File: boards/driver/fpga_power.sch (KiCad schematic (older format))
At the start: 6 parts

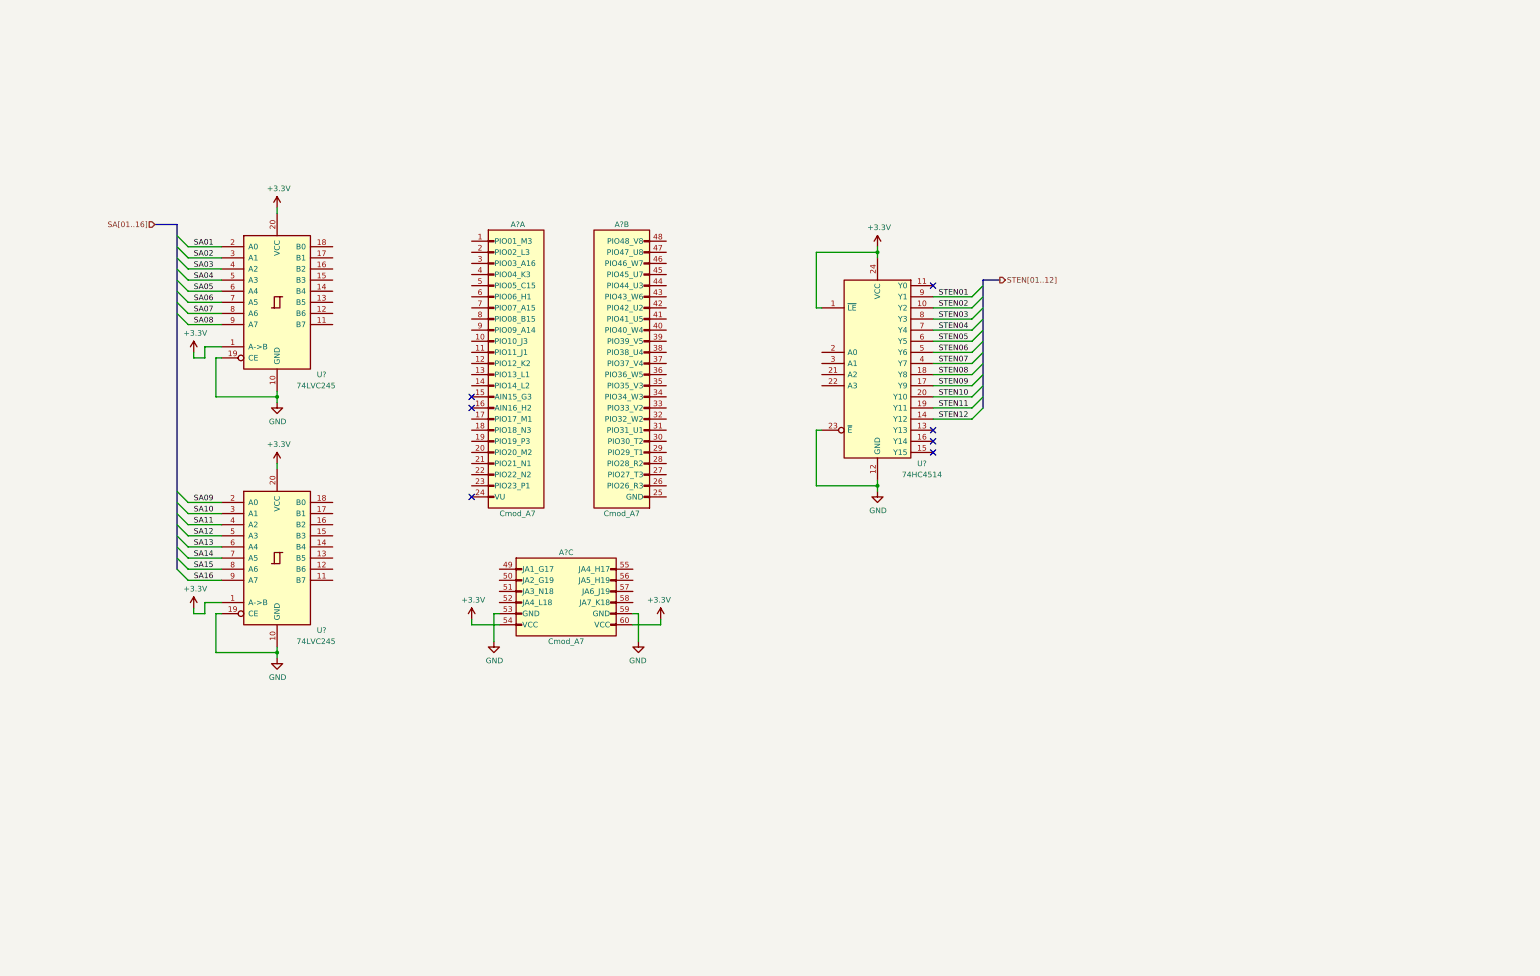
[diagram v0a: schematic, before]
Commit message: Driver boards: filled out all of the FPGA connections. Power circuits to still be defined.
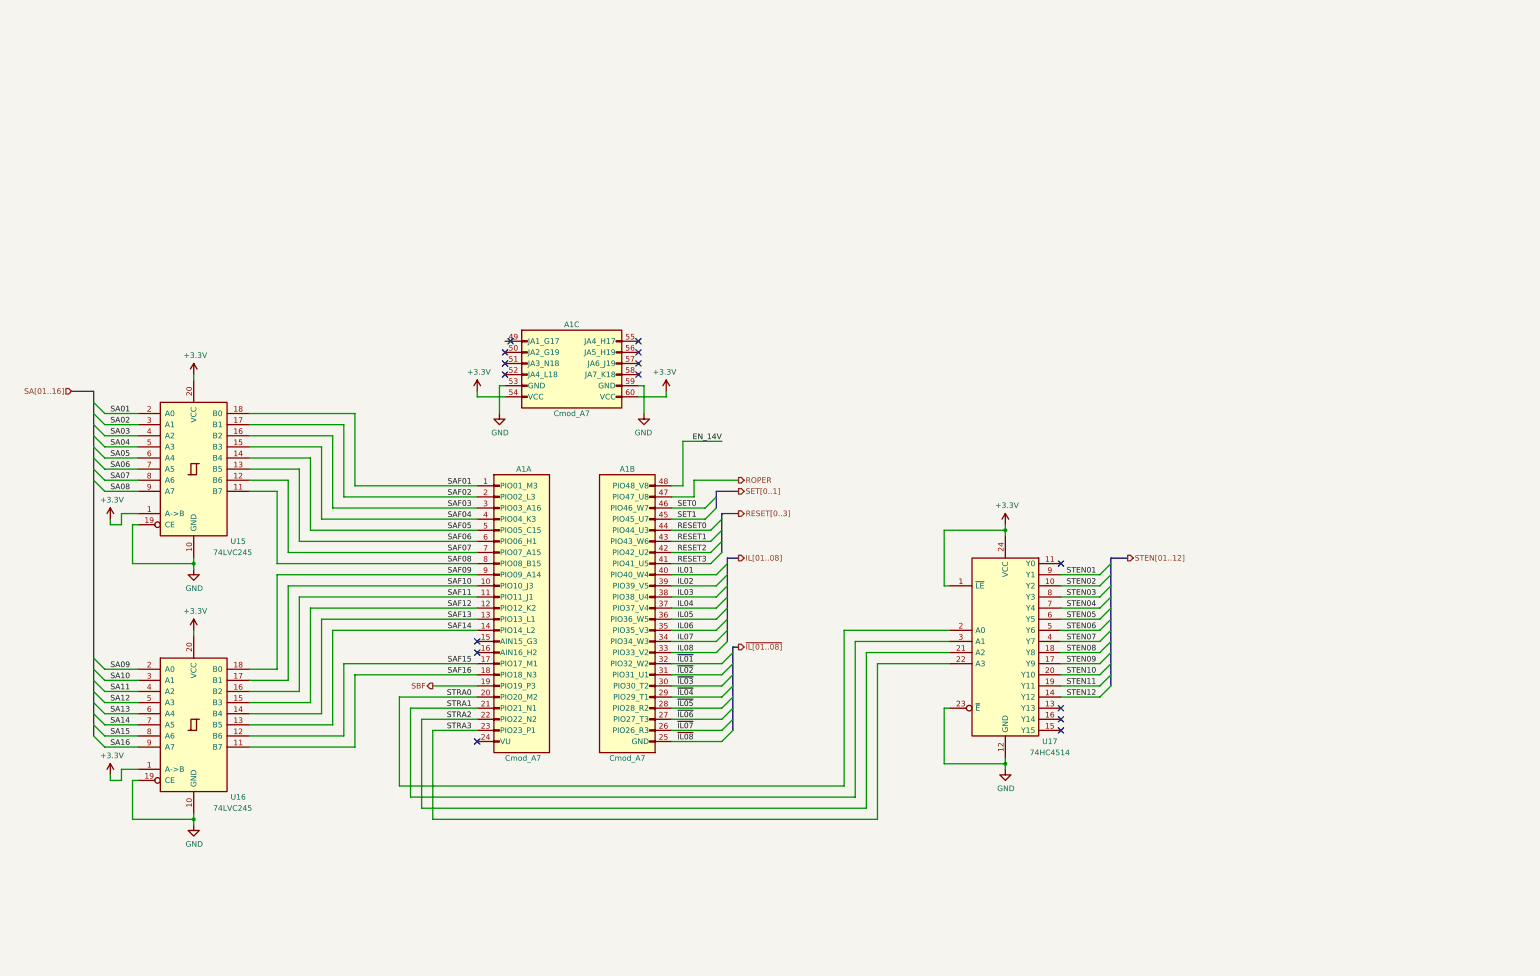
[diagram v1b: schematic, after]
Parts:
- gave numbers to parts that had none: 4
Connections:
- net SAF01: now reaches A1.1 (PIO01_M3)
- net SAF01: now also U15.18 (B0)
- net SAF10: now reaches A1.10 (PIO10_J3)
- net SAF10: now also U16.17 (B1)
- net SAF11: now reaches A1.11 (PIO11_J1)
- net SAF11: now also U16.16 (B2)
- net SAF12: now reaches A1.12 (PIO12_K2)
- net SAF12: now also U16.15 (B3)
- net SAF13: now reaches A1.13 (PIO13_L1)
- net SAF13: now also U16.14 (B4)
- net SAF14: now reaches A1.14 (PIO14_L2)
- net SAF14: now also U16.13 (B5)
- net SAF15: now reaches A1.17 (PIO17_M1)
- net SAF15: now also U16.12 (B6)
- net SAF16: now reaches A1.18 (PIO18_N3)
- net SAF16: now also U16.11 (B7)
- net SBF: now reaches A1.19 (PIO19_P3)
- net SAF02: now reaches A1.2 (PIO02_L3)
- net SAF02: now also U15.17 (B1)
- net STRA0: now reaches A1.20 (PIO20_M2)
- net STRA0: now also U17.2 (A0)
- net STRA1: now reaches A1.21 (PIO21_N1)
- net STRA1: now also U17.3 (A1)
- net STRA2: now reaches A1.22 (PIO22_N2)
- net STRA2: now also U17.21 (A2)
- net STRA3: now reaches A1.23 (PIO23_P1)
- net STRA3: now also U17.22 (A3)
- net SAF03: now reaches A1.3 (PIO03_A16)
- net SAF03: now also U15.16 (B2)
- net SAF04: now reaches A1.4 (PIO04_K3)
- net SAF04: now also U15.15 (B3)
- net SAF05: now reaches A1.5 (PIO05_C15)
- net SAF05: now also U15.14 (B4)
- net SAF06: now reaches A1.6 (PIO06_H1)
- net SAF06: now also U15.13 (B5)
- net SAF07: now reaches A1.7 (PIO07_A15)
- net SAF07: now also U15.12 (B6)
- net SAF08: now reaches A1.8 (PIO08_B15)
- net SAF08: now also U15.11 (B7)
- net SAF09: now reaches A1.9 (PIO09_A14)
- net SAF09: now also U16.18 (B0)
- net ~IL08: now reaches A1.25 (GND)
- net ~IL07: now reaches A1.26 (PIO26_R3)
- net ~IL06: now reaches A1.27 (PIO27_T3)
- net ~IL05: now reaches A1.28 (PIO28_R2)
- net ~IL04: now reaches A1.29 (PIO29_T1)
- net ~IL03: now reaches A1.30 (PIO30_T2)
- net ~IL02: now reaches A1.31 (PIO31_U1)
- net ~IL01: now reaches A1.32 (PIO32_W2)
- net IL08: now reaches A1.33 (PIO33_V2)
- net IL07: now reaches A1.34 (PIO34_W3)
- net IL06: now reaches A1.35 (PIO35_V3)
- net IL05: now reaches A1.36 (PIO36_W5)
- net IL04: now reaches A1.37 (PIO37_V4)
- net IL03: now reaches A1.38 (PIO38_U4)
- net IL02: now reaches A1.39 (PIO39_V5)
- net IL01: now reaches A1.40 (PIO40_W4)
- net RESET3: now reaches A1.41 (PIO41_U5)
- net RESET2: now reaches A1.42 (PIO42_U2)
- net RESET1: now reaches A1.43 (PIO43_W6)
- net RESET0: now reaches A1.44 (PIO44_U3)
- net SET1: now reaches A1.45 (PIO45_U7)
- net SET0: now reaches A1.46 (PIO46_W7)
- net ROPER: now reaches A1.47 (PIO47_U8)
- net EN_14V: now reaches A1.48 (PIO48_V8)
- no-connect marks 7 -> 15
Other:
- moved on the sheet: A1A, A1B, A1C, U15, U16, U17

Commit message: Completely overhauled rope driver circuitry to much, much more closely resemble the original.
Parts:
- added U11, U12, U13, U14: 74LVC2G04, symbol lachesis:74LVC2G04
- renumbered U16 to U10, U17 to U15, U15 to U9
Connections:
- net RESET0 is gone; now on net RESET1: A1.44 (PIO44_U3)
- net SET0 is gone; now on net SET1: A1.46 (PIO46_W7)
- net +3V3: now also U11.5 (VCC), U12.5 (VCC), U13.5 (VCC), U14.5 (VCC)
- net GND: now also A1.25 (GND), U11.2 (GND), U12.2 (GND), U13.2 (GND), U14.2 (GND)
- net IL01: now also U11.1
- net IL02: now also U11.3
- net IL03: now also U12.1
- net IL04: now also U12.3
- net IL05: now also U13.1
- net IL06: now also U13.3
- net IL07: now also U14.1
- net IL08: now also U14.3
- net RESET1: no longer A1.43 (PIO43_W6)
- net RESET2: now also A1.43 (PIO43_W6); no longer A1.42 (PIO42_U2)
- net RESET3: now also A1.42 (PIO42_U2); no longer A1.41 (PIO41_U5)
- net SET1: no longer A1.45 (PIO45_U7)
- net STRA0: now also A1.31 (PIO31_U1); no longer A1.20 (PIO20_M2)
- net STRA1: now also A1.30 (PIO30_T2); no longer A1.21 (PIO21_N1)
- net STRA2: now also A1.29 (PIO29_T1); no longer A1.22 (PIO22_N2)
- net STRA3: now also A1.28 (PIO28_R2); no longer A1.23 (PIO23_P1)
- net ~IL01: now also U11.6; no longer A1.32 (PIO32_W2)
- net ~IL02: now also U11.4; no longer A1.31 (PIO31_U1)
- net ~IL03: now also U12.6; no longer A1.30 (PIO30_T2)
- net ~IL04: now also U12.4; no longer A1.29 (PIO29_T1)
- net ~IL05: now also U13.6; no longer A1.28 (PIO28_R2)
- net ~IL06: now also U13.4; no longer A1.27 (PIO27_T3)
- net ~IL07: now also U14.6; no longer A1.26 (PIO26_R3)
- net ~IL08: now also U14.4; no longer A1.25 (GND)
- new net IHENV: A1.32 (PIO32_W2)
- new net RESET4: A1.41 (PIO41_U5)
- new net SET2: A1.45 (PIO45_U7)
- no-connect marks 15 -> 21
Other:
- moved on the sheet: A1A, A1B, A1C, U10, U15, U9

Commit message: Driver board: a bit more schematic work and some initial footprint selections
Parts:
- U10, U9: footprint (none) -> Package_SO:TSSOP-20_4.4x6.5mm_P0.65mm
- U11, U12, U13, U14: footprint (none) -> Package_TO_SOT_SMD:SOT-23-6
- U15: footprint (none) -> Package_SO:SOIC-24W_7.5x15.4mm_P1.27mm
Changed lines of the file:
@@
 F 0 "U9" H 3800 5500 50  0000 C CNN
 F 1 "74LVC245" H 3750 5400 50  0000 C CNN
-F 2 "" H 3400 6150 50  0001 C CNN
+F 2 "Package_SO:TSSOP-20_4.4x6.5mm_P0.65mm" H 3400 6150 50  0001 C CNN
 F 3 "http://www.ti.com/lit/gpn/sn74HC245" H 3400 6150 50  0001 C CNN
 	1    3400 6150
@@
 F 0 "U10" H 3800 7800 50  0000 C CNN
 F 1 "74LVC245" H 3750 7700 50  0000 C CNN
-F 2 "" H 3400 8450 50  0001 C CNN
+F 2 "Package_SO:TSSOP-20_4.4x6.5mm_P0.65mm" H 3400 8450 50  0001 C CNN
 F 3 "http://www.ti.com/lit/gpn/sn74HC245" H 3400 8450 50  0001 C CNN
 	1    3400 8450
@@
 F 0 "U15" H 10600 7300 50  0000 C CNN
 F 1 "74HC4514" H 10600 7200 50  0000 C CNN
-F 2 "" H 10200 8150 50  0001 C CNN
+F 2 "Package_SO:SOIC-24W_7.5x15.4mm_P1.27mm" H 10200 8150 50  0001 C CNN
 F 3 "" H 10200 8150 50  0001 C CNN
 	1    10200 8150
@@
 F 0 "U11" H 10150 4400 50  0000 C CNN
 F 1 "74LVC2G04" H 10300 4200 50  0000 C CNN
-F 2 "" H 10100 4300 50  0001 C CNN
+F 2 "Package_TO_SOT_SMD:SOT-23-6" H 10100 4300 50  0001 C CNN
 F 3 "http://www.ti.com/lit/sg/scyt129e/scyt129e.pdf" H 10100 4300 50  0001 C CNN
 	1    10100 4300
@@
 F 0 "U11" H 10150 4700 50  0000 C CNN
 F 1 "74LVC2G04" H 10300 4500 50  0000 C CNN
-F 2 "" H 10100 4600 50  0001 C CNN
+F 2 "Package_TO_SOT_SMD:SOT-23-6" H 10100 4600 50  0001 C CNN
 F 3 "http://www.ti.com/lit/sg/scyt129e/scyt129e.pdf" H 10100 4600 50  0001 C CNN
 	2    10100 4600
@@
 F 0 "U12" H 10150 5000 50  0000 C CNN
 F 1 "74LVC2G04" H 10300 4800 50  0000 C CNN
-F 2 "" H 10100 4900 50  0001 C CNN
+F 2 "Package_TO_SOT_SMD:SOT-23-6" H 10100 4900 50  0001 C CNN
 F 3 "http://www.ti.com/lit/sg/scyt129e/scyt129e.pdf" H 10100 4900 50  0001 C CNN
 	1    10100 4900
@@
 F 0 "U12" H 10150 5300 50  0000 C CNN
 F 1 "74LVC2G04" H 10300 5100 50  0000 C CNN
-F 2 "" H 10100 5200 50  0001 C CNN
+F 2 "Package_TO_SOT_SMD:SOT-23-6" H 10100 5200 50  0001 C CNN
 F 3 "http://www.ti.com/lit/sg/scyt129e/scyt129e.pdf" H 10100 5200 50  0001 C CNN
 	2    10100 5200
@@
 F 0 "U13" H 10150 5600 50  0000 C CNN
 F 1 "74LVC2G04" H 10300 5400 50  0000 C CNN
-F 2 "" H 10100 5500 50  0001 C CNN
+F 2 "Package_TO_SOT_SMD:SOT-23-6" H 10100 5500 50  0001 C CNN
 F 3 "http://www.ti.com/lit/sg/scyt129e/scyt129e.pdf" H 10100 5500 50  0001 C CNN
 	1    10100 5500
@@
 F 0 "U13" H 10150 5900 50  0000 C CNN
 F 1 "74LVC2G04" H 10300 5700 50  0000 C CNN
-F 2 "" H 10100 5800 50  0001 C CNN
+F 2 "Package_TO_SOT_SMD:SOT-23-6" H 10100 5800 50  0001 C CNN
 F 3 "http://www.ti.com/lit/sg/scyt129e/scyt129e.pdf" H 10100 5800 50  0001 C CNN
 	2    10100 5800
@@
 F 0 "U14" H 10150 6200 50  0000 C CNN
 F 1 "74LVC2G04" H 10300 6000 50  0000 C CNN
-F 2 "" H 10100 6100 50  0001 C CNN
+F 2 "Package_TO_SOT_SMD:SOT-23-6" H 10100 6100 50  0001 C CNN
 F 3 "http://www.ti.com/lit/sg/scyt129e/scyt129e.pdf" H 10100 6100 50  0001 C CNN
 	1    10100 6100
@@
 F 0 "U14" H 10150 6500 50  0000 C CNN
 F 1 "74LVC2G04" H 10300 6300 50  0000 C CNN
-F 2 "" H 10100 6400 50  0001 C CNN
+F 2 "Package_TO_SOT_SMD:SOT-23-6" H 10100 6400 50  0001 C CNN
 F 3 "http://www.ti.com/lit/sg/scyt129e/scyt129e.pdf" H 10100 6400 50  0001 C CNN
 	2    10100 6400
@@
 F 0 "U11" H 13200 8500 50  0000 L CNN
 F 1 "74LVC2G04" H 13100 8400 50  0000 L CNN
-F 2 "" H 13300 8400 50  0001 C CNN
+F 2 "Package_TO_SOT_SMD:SOT-23-6" H 13300 8400 50  0001 C CNN
 F 3 "http://www.ti.com/lit/sg/scyt129e/scyt129e.pdf" H 13300 8400 50  0001 C CNN
 	3    13300 8400
@@
 F 0 "U12" H 13800 8500 50  0000 L CNN
 F 1 "74LVC2G04" H 13700 8400 50  0000 L CNN
-F 2 "" H 13900 8400 50  0001 C CNN
+F 2 "Package_TO_SOT_SMD:SOT-23-6" H 13900 8400 50  0001 C CNN
 F 3 "http://www.ti.com/lit/sg/scyt129e/scyt129e.pdf" H 13900 8400 50  0001 C CNN
 	3    13900 8400
@@
 F 0 "U13" H 14400 8500 50  0000 L CNN
 F 1 "74LVC2G04" H 14300 8400 50  0000 L CNN
-F 2 "" H 14500 8400 50  0001 C CNN
+F 2 "Package_TO_SOT_SMD:SOT-23-6" H 14500 8400 50  0001 C CNN
 F 3 "http://www.ti.com/lit/sg/scyt129e/scyt129e.pdf" H 14500 8400 50  0001 C CNN
 	3    14500 8400
@@
 F 0 "U14" H 15000 8500 50  0000 L CNN
 F 1 "74LVC2G04" H 14900 8400 50  0000 L CNN
-F 2 "" H 15100 8400 50  0001 C CNN
+F 2 "Package_TO_SOT_SMD:SOT-23-6" H 15100 8400 50  0001 C CNN
 F 3 "http://www.ti.com/lit/sg/scyt129e/scyt129e.pdf" H 15100 8400 50  0001 C CNN
 	3    15100 8400

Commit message: Driver board: finished first rough draft schematic. Lots of placeholders, but at least every place is held.
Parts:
- added C29, C30, C33, C34, C35, C36, C37: 0.1uF, symbol Device:C_Small
- added C31: 0.68uF, symbol Device:C
- added C32: 10nF, symbol Device:C
- added D160: D_Zener_ALT, symbol Device:D_Zener_ALT
- added J1: Barrel_Jack, symbol Connector:Barrel_Jack
- added Q90: IRF530, symbol Device:Q_NMOS_DGS
- added R230: 0.01, symbol Device:R_US
- added R231: 10, symbol Device:R_US
- added R232: 1k, symbol Device:R_US
- added R233: 59k, symbol Device:R_US
- added R234: 3.57k, symbol Device:R_US
- added U11: JTE0624D05, Converter_DCDC:Converter_DCDC_XP_POWER_JTExxxxDxx_THT, symbol Converter_DCDC:JTE0624D05
- added U12: LT1641-1, Package_SO:SOIC-8_3.9x4.9mm_P1.27mm, symbol Power_Management:LT1641-1
- renumbered U15 to U13, U11 to U14, U12 to U15, U13 to U16, U14 to U17
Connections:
- net labels added: +14V, +5V, -5V, IL1, IL2, IL3, IL4, IL5, IL6, IL7, IL8, IL[1..8], PG_14V, SA1, SA2, SA3, SA4, SA5, SA6, SA7, SA8, SA9, SAF1, SAF2, SAF3, SAF4, SAF5, SAF6, SAF7, SAF8, SAF9, SA[1..16], STEN1, STEN2, STEN3, STEN4, STEN5, STEN6, STEN7, STEN8, STEN9, STEN[1..12], ~IL1, ~IL2, ~IL3, ~IL4, ~IL5, ~IL6, ~IL7, ~IL8, ~IL[1..8]
- net labels removed: IL01, IL02, IL03, IL04, IL05, IL06, IL07, IL08, IL[01..08], SA01, SA02, SA03, SA04, SA05, SA06, SA07, SA08, SA09, SAF01, SAF02, SAF03, SAF04, SAF05, SAF06, SAF07, SAF08, SAF09, SA[01..16], STEN01, STEN02, STEN03, STEN04, STEN05, STEN06, STEN07, STEN08, STEN09, STEN[01..12], ~IL01, ~IL02, ~IL03, ~IL04, ~IL05, ~IL06, ~IL07, ~IL08, ~IL[01..08]
- wire segments 176 -> 258
- no-connect marks 21 -> 20
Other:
- note added: "FIXME: This is all reference design stuff! Everything is wrong!"
- moved on the sheet: A1A, A1B, A1C, U10, U13, U14A, U14B, U14C, U15A, U15B, U15C, U16A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

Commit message: Driver board: fleshed out the hotswap controller, tweaked some resistors, and added some bypass caps
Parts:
- removed C31: 0.68uF, symbol Device:C
- removed C32: 10nF, symbol Device:C
- removed D160: D_Zener_ALT, symbol Device:D_Zener_ALT
- removed R231: 10, symbol Device:R_US
- removed R232: 1k, symbol Device:R_US
- removed R233: 59k, symbol Device:R_US
- removed R234: 3.57k, symbol Device:R_US
- removed U12: LT1641-1, Package_SO:SOIC-8_3.9x4.9mm_P1.27mm, symbol Power_Management:LT1641-1
- added C47: 0.33uF, symbol Device:C
- added C48: 10nF, symbol Device:C
- added R230: 1020k, symbol Device:R_Small_US
- added R231: 2.87k, symbol Device:R_Small_US
- added R232: 9.76k, symbol Device:R_Small_US
- added R233: 54.9k, symbol Device:R_Small_US
- added R235: 10, symbol Device:R_US
- added R236: 1k, symbol Device:R_US
- added R237, R238: 10k, symbol Device:R_US
- added U12: LTC4231-1, symbol lachesis:LTC4231-1
- R234: renamed from R230; value 0.01 -> 0.025
- renumbered C29 to C45, C30 to C46, C33 to C49, C34 to C50, C35 to C51, C36 to C52, C37 to C53
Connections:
- wire segments 258 -> 256
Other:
- note added: "Vov (@ 15.75V) = 15.75*(54.9k/(1020k+2.87k+9.76k+54.9k)) = 0.795V\nVuvl (@ 12.80V) = 12.80*(2.87k+9.76k+54.9k)/(1020k+2.87k+9.76k+54.9k) = 0.795V"
- note removed: "FIXME: This is all reference design stuff! Everything is wrong!"
